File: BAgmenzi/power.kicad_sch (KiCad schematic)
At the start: 37 parts, among them J2 DF52-2S-0.8H(21), J3 USB3076-30-A, U10 PESD1USB30, U11 MAX77654BENV+T, U13 TPS7A2033DBVDQN, U14 TPS63900

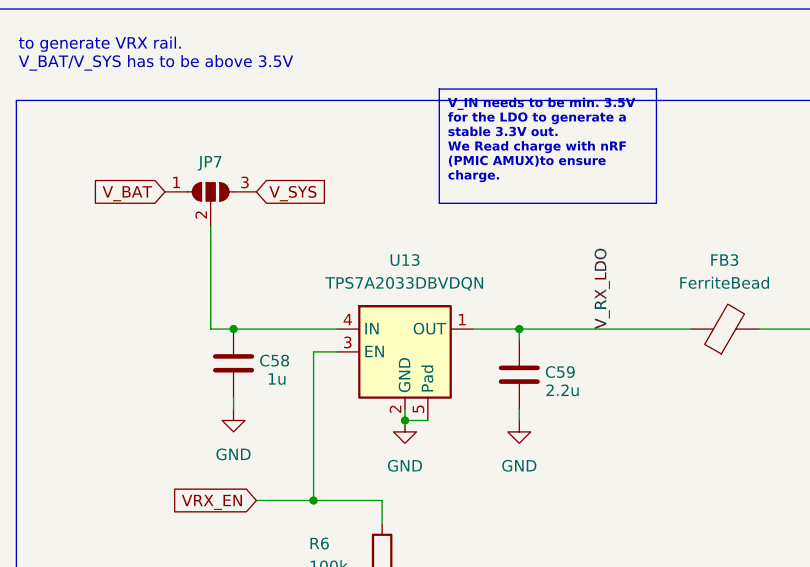
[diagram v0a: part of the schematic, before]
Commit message: LCSC parts complete, changed L5andL6 footprint
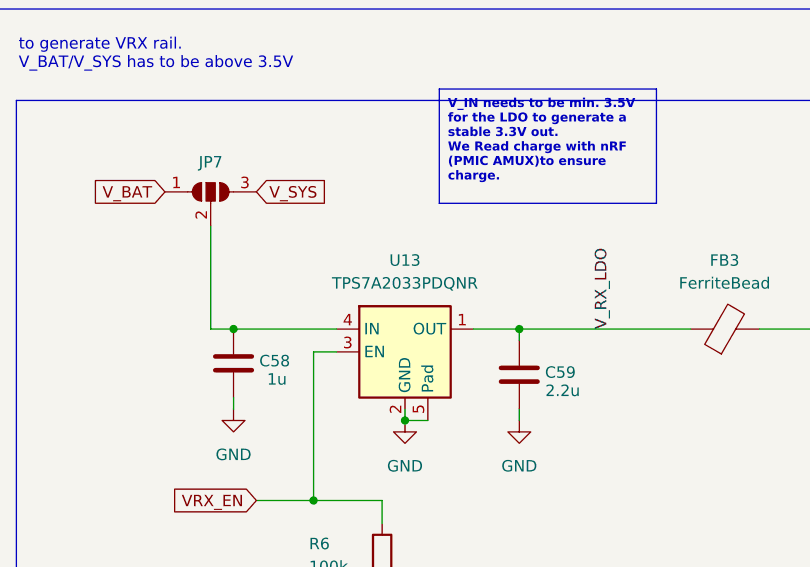
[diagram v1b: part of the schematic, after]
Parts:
- C32: LCSC Part # C161362 -> C169842
- C47, C52, C54: LCSC Part # (none) -> C105226
- C49, C51, C58: LCSC Part # C20441333 -> C14445
- C53: LCSC Part # C2190182 -> C26404
- C56: LCSC Part # C15525 -> (none)
- C59: LCSC Part # C12530 -> C77002
- C60: LCSC Part # C1713 -> C408132
- D4: LCSC Part # C145508 -> C145508
- FB3: footprint PCB1:FP-BLM18-0_15-t0_8-IPC_A -> Inductor_SMD:L_0603_1608Metric; LCSC Part # (none) -> C3717002
- J2: LCSC Part # C82431 -> C82431
- J3: LCSC Part # C6007475 -> C6007475
- L7: LCSC Part # (none) -> C2891571
- R32, R33: LCSC Part # C423829 -> C25900
- R34, R35, R6: LCSC Part # C723496 -> C192169
- R36: LCSC Part # C270305 -> C191984
- RT1: LCSC Part # (none) -> C77131
- S1: LCSC Part # C2760983 -> C2760983
- U13: value TPS7A2033DBVDQN -> TPS7A2033PDQNR; LCSC Part # (none) -> C2871641
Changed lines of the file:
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@@
 			)
 		)
-		(property "LCSC Part #" "C2190182"
+		(property "LCSC Part #" "C26404 "
 			(at 213.36 146.05 90)
 			(effects
@@
 			)
 		)
-		(property "LCSC Part #" "C723496"
+		(property "LCSC Part #" "C192169 "
 			(at 68.58 154.94 0)
 			(effects
@@
 			)
 		)
-		(property "Value" "TPS7A2033DBVDQN"
+		(property "Value" "TPS7A2033PDQNR"
 			(at 170.18 238.76 0)
 			(effects
@@
 			)
 		)
+		(property "LCSC Part #" "C2871641 "
+			(at 170.18 246.38 0)
+			(effects
+				(font
+					(size 1.27 1.27)
+				)
+				(hide yes)
+			)
+		)
 		(pin "4"
 		)
@@
 			)
 		)
-		(property "LCSC Part #" "C145508"
+		(property "LCSC Part #" "C145508 "
 			(at 105.41 43.18 0)
 			(effects
@@
 			)
 		)
-		(property "LCSC Part #" "C12530"
+		(property "LCSC Part #" "C77002 "
 			(at 182.88 248.92 0)
 			(effects
@@
 			)
 		)
-		(property "LCSC Part #" "C1713"
+		(property "LCSC Part #" "C408132 "
 			(at 219.71 252.73 0)
 			(effects
@@
 			)
 		)
+		(property "LCSC Part #" "C105226 "
+			(at 193.04 137.16 0)
+			(effects
+				(font
+					(size 1.27 1.27)
+				)
+				(hide yes)
+			)
+		)
 		(pin "2"
 		)
@@
 			)
 		)
-		(property "Footprint" "PCB1:FP-BLM18-0_15-t0_8-IPC_A"
+		(property "Footprint" "Inductor_SMD:L_0603_1608Metric"
 			(at 205.74 245.618 90)
 			(effects
@@
 			)
 		)
+		(property "LCSC Part #" "C3717002 "
+			(at 205.74 243.84 90)
+			(effects
+				(font
+					(size 1.27 1.27)
+				)
+				(hide yes)
+			)
+		)
 		(pin "1"
 		)
@@
 			)
 		)
+		(property "LCSC Part #" "C77131 "
+			(at 154.94 173.99 0)
+			(effects
+				(font
+					(size 1.27 1.27)
+				)
+				(hide yes)
+			)
+		)
 		(pin "1"
 		)
@@
 			)
 		)
+		(property "LCSC Part #" "C105226 "
+			(at 278.13 123.19 90)
+			(effects
+				(font
+					(size 1.27 1.27)
+				)
+				(hide yes)
+			)
+		)
 		(pin "2"
 		)
@@
 			)
 		)
-		(property "LCSC Part #" "C723496"
+		(property "LCSC Part #" "C192169 "
 			(at 167.64 269.24 0)
 			(effects
@@
 			)
 		)
-		(property "LCSC Part #" "C15525"
+		(property "LCSC Part #" ""
 			(at 54.61 323.85 0)
 			(effects
@@
 			)
 		)
-		(property "LCSC Part #" "C6007475"
+		(property "LCSC Part #" "C6007475 "
 			(at 142.24 52.07 0)
 			(effects
@@
 			)
 		)
-		(property "LCSC Part #" "C20441333"
+		(property "LCSC Part #" "C14445 "
 			(at 265.43 127 0)
 			(effects
@@
 			)
 		)
-		(property "LCSC Part #" "C423829"
+		(property "LCSC Part #" "C25900 "
 			(at 96.52 153.67 0)
 			(effects
@@
 			)
 		)
-		(property "LCSC Part #" "C2760983"
+		(property "LCSC Part #" "C2760983 "
 			(at 69.85 184.15 0)
 			(effects
@@
 			)
 		)
-		(property "LCSC Part #" "C82431"
+		(property "LCSC Part #" "C82431 "
 			(at 198.12 36.83 0)
 			(effects
@@
 			)
 		)
-		(property "LCSC Part #" "C20441333"
+		(property "LCSC Part #" "C14445 "
 			(at 151.13 247.65 0)
 			(effects
@@
 			)
 		)
-		(property "LCSC Part #" "C723496"
+		(property "LCSC Part #" "C192169 "
 			(at 58.42 154.94 0)
 			(effects
@@
 			)
 		)
-		(property "LCSC Part #" "C270305"
+		(property "LCSC Part #" "C191984 "
 			(at 156.21 166.37 90)
 			(effects
@@
 			)
 		)
+		(property "LCSC Part #" "C2891571 "
+			(at 213.36 138.43 0)
+			(effects
+				(font
+					(size 1.27 1.27)
+				)
+				(hide yes)
+			)
+		)
 		(pin "1"
 		)
@@
 			)
 		)
-		(property "LCSC Part #" "C20441333"
+		(property "LCSC Part #" "C14445 "
 			(at 158.75 129.54 0)
 			(effects
@@
 			)
 		)
-		(property "LCSC Part #" "C161362"
+		(property "LCSC Part #" "C169842 "
 			(at 279.4 152.4 0)
 			(effects
@@
 			)
 		)
-		(property "LCSC Part #" "C423829"
+		(property "LCSC Part #" "C25900 "
 			(at 101.6 153.67 0)
 			(effects
@@
 			(at 269.24 152.4 0)
 			(effects
+				(font
+					(size 1.27 1.27)
+				)
+				(hide yes)
+			)
+		)
+		(property "LCSC Part #" "C105226 "
+			(at 269.24 152.4 0)
+			(effects

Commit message: corrected LCSC numbers, other changes, Testpoints
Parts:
- added DVDD1, VRX1: TestPoint, TestPoint:TestPoint_Pad_D1.0mm, symbol Connector:TestPoint
- C32: LCSC Part # C169842 -> C1525
- C47, C52, C54: LCSC Part # C105226 -> C105226
- C49, C51, C58: LCSC Part # C14445 -> C14445
- C53: LCSC Part # C26404 -> C26404
- C59: LCSC Part # C77002 -> C77002
- C60: LCSC Part # C408132 -> C408132
- D4: LCSC Part # C145508 -> C145508
- FB3: LCSC Part # C3717002 -> C3717002
- J2: LCSC Part # C82431 -> C82431
- J3: LCSC Part # C6007475 -> C6007475
- L7: LCSC Part # C2891571 -> C2891571
- R32, R33: LCSC Part # C25900 -> C25900
- R34, R35, R6: LCSC Part # C192169 -> C192169
- R36: LCSC Part # C191984 -> C191984
- RT1: LCSC Part # C77131 -> C77131
- S1: LCSC Part # C2760983 -> C2760983
- U13: LCSC Part # C2871641 -> C2871641
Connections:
- net DVDD_3.3: now also DVDD1.1
- net V_RX: now also VRX1.1
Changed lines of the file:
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@@
 	)
 	(junction
+		(at 273.05 107.95)
+		(diameter 0)
+		(color 0 0 0 0)
+	)
+	(junction
 		(at 58.42 166.37)
 		(diameter 0)
@@
 	)
 	(junction
+		(at 236.22 243.84)
+		(diameter 0)
+		(color 0 0 0 0)
+	)
+	(junction
 		(at 160.02 262.89)
 		(diameter 0)
@@
 	)
 	(junction
+		(at 273.05 114.3)
+		(diameter 0)
+		(color 0 0 0 0)
+	)
+	(junction
 		(at 203.2 140.97)
 		(diameter 0)
@@
 	(wire
 		(pts
+			(xy 236.22 243.84) (xy 243.84 243.84)
+		)
+		(stroke
+			(width 0)
+			(type default)
+		)
+	)
+	(wire
+		(pts
 			(xy 58.42 166.37) (xy 107.95 166.37)
 		)
@@
 	(wire
 		(pts
-			(xy 162.56 118.11) (xy 148.59 118.11)
+			(xy 148.59 118.11) (xy 162.56 118.11)
 		)
 		(stroke
@@
 	(wire
 		(pts
+			(xy 273.05 107.95) (xy 273.05 105.41)
+		)
+		(stroke
+			(width 0)
+			(type default)
+		)
+	)
+	(wire
+		(pts
 			(xy 72.39 52.07) (xy 59.69 52.07)
 		)
@@
 	(wire
 		(pts
-			(xy 219.71 243.84) (xy 243.84 243.84)
+			(xy 219.71 243.84) (xy 236.22 243.84)
 		)
 		(stroke
@@
 	(wire
 		(pts
+			(xy 273.05 107.95) (xy 273.05 114.3)
+		)
+		(stroke
+			(width 0)
+			(type default)
+		)
+	)
+	(wire
+		(pts
 			(xy 142.24 58.42) (xy 142.24 57.15)
 		)
@@
 	(wire
 		(pts
+			(xy 271.78 114.3) (xy 273.05 114.3)
+		)
+		(stroke
+			(width 0)
+			(type default)
+		)
+	)
+	(wire
+		(pts
 			(xy 106.68 344.17) (xy 106.68 346.71)
 		)
@@
 	(wire
 		(pts
-			(xy 273.05 123.19) (xy 273.05 105.41)
+			(xy 273.05 123.19) (xy 273.05 114.3)
 		)
 		(stroke
@@
 	)
 	(label "DVDD_3.3"
-		(at 273.05 110.49 180)
+		(at 271.78 114.3 180)
 		(effects
 			(font
@@
 			)
 		)
-		(property "LCSC Part #" "C26404 "
+		(property "LCSC Part #" "C26404"
 			(at 213.36 146.05 90)
 			(effects
@@
 			)
 		)
-		(property "LCSC Part #" "C192169 "
+		(property "LCSC Part #" "C192169"
 			(at 68.58 154.94 0)
 			(effects
@@
 	)
 	(symbol
+		(lib_id "Connector:TestPoint")
+		(at 236.22 243.84 0)
+		(unit 1)
+		(exclude_from_sim no)
+		(in_bom yes)
+		(on_board yes)
+		(dnp no)
+		(fields_autoplaced yes)
+		(property "Reference" "VRX1"
+			(at 238.76 239.2679 0)
+			(effects
+				(font
+					(size 1.27 1.27)
+				)
+				(justify left)
+			)
+		)
+		(property "Value" "TestPoint"
+			(at 238.76 241.8079 0)
+			(effects
+				(font
+					(size 1.27 1.27)
+				)
+				(justify left)
+			)
+		)
+		(property "Footprint" "TestPoint:TestPoint_Pad_D1.0mm"
+			(at 241.3 243.84 0)
+			(effects
+				(font
+					(size 1.27 1.27)
+				)
+				(hide yes)
+			)
+		)
+		(property "Datasheet" "~"
+			(at 241.3 243.84 0)
+			(effects
+				(font
+					(size 1.27 1.27)
+				)
+				(hide yes)
+			)
+		)
+		(property "Description" "test point"
+			(at 236.22 243.84 0)
+			(effects
+				(font
+					(size 1.27 1.27)
+				)
+				(hide yes)
+			)
+		)
+		(pin "1"
+		)
+		(instances
+			(project ""
+				(path "/8cc4acae-3f14-463c-b0a0-3bc1c8d05954/d463870e-9fcf-4af5-ace7-dfb7bf5f63b9"
+					(reference "VRX1")
+					(unit 1)
+				)
+			)
+		)
+	)
+	(symbol
 		(lib_id "EEG_SchLib:MAX77654BENV+T")
 		(at 243.84 135.89 0)
@@
 			)
 		)
-		(property "LCSC Part #" "C2871641 "
+		(property "LCSC Part #" "C2871641"
 			(at 170.18 246.38 0)
 			(effects
@@
 			)
 		)
-		(property "LCSC Part #" "C145508 "
+		(property "LCSC Part #" "C145508"
 			(at 105.41 43.18 0)
 			(effects
@@
 			)
 		)
-		(property "LCSC Part #" "C77002 "
+		(property "LCSC Part #" "C77002"
 			(at 182.88 248.92 0)
 			(effects
@@
 			)
 		)
-		(property "LCSC Part #" "C408132 "
+		(property "LCSC Part #" "C408132"
 			(at 219.71 252.73 0)
 			(effects
@@
 			)
 		)
-		(property "LCSC Part #" "C105226 "
+		(property "LCSC Part #" "C105226"
 			(at 193.04 137.16 0)
 			(effects
@@
 			)
 		)
-		(property "LCSC Part #" "C3717002 "
+		(property "LCSC Part #" "C3717002"
 			(at 205.74 243.84 90)
 			(effects
@@
 	)
 	(symbol
+		(lib_id "Connector:TestPoint")
+		(at 273.05 107.95 90)
+		(unit 1)
+		(exclude_from_sim no)
+		(in_bom yes)
+		(on_board yes)
+		(dnp no)
+		(fields_autoplaced yes)
+		(property "Reference" "DVDD1"
+			(at 269.748 102.87 90)
+			(effects
+				(font
+					(size 1.27 1.27)
+				)
+			)
+		)
+		(property "Value" "TestPoint"
+			(at 269.748 105.41 90)
+			(effects
+				(font
+					(size 1.27 1.27)
+				)
+			)
+		)
+		(property "Footprint" "TestPoint:TestPoint_Pad_D1.0mm"
+			(at 273.05 102.87 0)
+			(effects
+				(font
+					(size 1.27 1.27)
+				)
+				(hide yes)
+			)
+		)
+		(property "Datasheet" "~"
+			(at 273.05 102.87 0)
+			(effects
+				(font
+					(size 1.27 1.27)
+				)
+				(hide yes)
+			)
+		)
+		(property "Description" "test point"
+			(at 273.05 107.95 0)
+			(effects
+				(font
+					(size 1.27 1.27)
+				)
+				(hide yes)
+			)
+		)
+		(pin "1"
+		)
+		(instances
+			(project "BAgmenzi"
+				(path "/8cc4acae-3f14-463c-b0a0-3bc1c8d05954/d463870e-9fcf-4af5-ace7-dfb7bf5f63b9"
+					(reference "DVDD1")
+					(unit 1)
+				)
+			)
+		)
+	)
+	(symbol
 		(lib_id "Device:R")
 		(at 95.25 350.52 180)
@@
 			)
 		)
-		(property "LCSC Part #" "C77131 "
+		(property "LCSC Part #" "C77131"
 			(at 154.94 173.99 0)
 			(effects
@@
 			)
 		)
-		(property "LCSC Part #" "C105226 "
+		(property "LCSC Part #" "C105226"
 			(at 278.13 123.19 90)
 			(effects
@@
 			)
 		)
-		(property "LCSC Part #" "C192169 "
+		(property "LCSC Part #" "C192169"
 			(at 167.64 269.24 0)
 			(effects
@@
 			)
 		)
-		(property "LCSC Part #" "C6007475 "
+		(property "LCSC Part #" "C6007475"
 			(at 142.24 52.07 0)
 			(effects
@@
 			)
 		)
-		(property "LCSC Part #" "C14445 "
+		(property "LCSC Part #" "C14445"
 			(at 265.43 127 0)
 			(effects
@@
 			)
 		)
-		(property "LCSC Part #" "C25900 "
+		(property "LCSC Part #" "C25900"
 			(at 96.52 153.67 0)
 			(effects
@@
 			)
 		)
-		(property "LCSC Part #" "C2760983 "
+		(property "LCSC Part #" "C2760983"
 			(at 69.85 184.15 0)
 			(effects
@@
 			)
 		)
-		(property "LCSC Part #" "C82431 "
+		(property "LCSC Part #" "C82431"
 			(at 198.12 36.83 0)
 			(effects
@@
 			)
 		)
-		(property "LCSC Part #" "C14445 "
+		(property "LCSC Part #" "C14445"
 			(at 151.13 247.65 0)
 			(effects
@@
 			)
 		)
-		(property "LCSC Part #" "C192169 "
+		(property "LCSC Part #" "C192169"
 			(at 58.42 154.94 0)
 			(effects
@@
 			)
 		)
-		(property "LCSC Part #" "C191984 "
+		(property "LCSC Part #" "C191984"
 			(at 156.21 166.37 90)
 			(effects
@@
 			)
 		)
-		(property "LCSC Part #" "C2891571 "
+		(property "LCSC Part #" "C2891571"
 			(at 213.36 138.43 0)
 			(effects
@@
 			)
 		)
-		(property "LCSC Part #" "C14445 "
+		(property "LCSC Part #" "C14445"
 			(at 158.75 129.54 0)
 			(effects
@@
 			)
 		)
-		(property "LCSC Part #" "C169842 "
+		(property "LCSC Part #" "C1525"
 			(at 279.4 152.4 0)
 			(effects
@@
 			)
 		)
-		(property "LCSC Part #" "C25900 "
+		(property "LCSC Part #" "C25900"
 			(at 101.6 153.67 0)
 			(effects
@@
 			)
 		)
-		(property "LCSC Part #" "C105226 "
+		(property "LCSC Part #" "C105226"
 			(at 269.24 152.4 0)
 			(effects

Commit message: small changes
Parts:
- added VLED1: TestPoint, TestPoint:TestPoint_Pad_D1.0mm, symbol Connector:TestPoint
- DVDD1, VRX1: now left out of the parts list
- U10: now not fitted
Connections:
- net V_LED: now also VLED1.1
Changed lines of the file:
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@@
 	)
 	(junction
+		(at 280.67 140.97)
+		(diameter 0)
+		(color 0 0 0 0)
+	)
+	(junction
 		(at 97.79 123.19)
 		(diameter 0)
@@
 	(wire
 		(pts
+			(xy 280.67 140.97) (xy 283.21 140.97)
+		)
+		(stroke
+			(width 0)
+			(type default)
+		)
+	)
+	(wire
+		(pts
 			(xy 78.74 143.51) (xy 78.74 163.83)
 		)
@@
 	(wire
 		(pts
-			(xy 279.4 140.97) (xy 283.21 140.97)
+			(xy 279.4 140.97) (xy 280.67 140.97)
 		)
 		(stroke
@@
 		(in_bom yes)
 		(on_board yes)
-		(dnp no)
+		(dnp yes)
 		(property "Reference" "U10"
 			(at 103.886 68.072 0)
@@
 		(unit 1)
 		(exclude_from_sim no)
-		(in_bom yes)
+		(in_bom no)
 		(on_board yes)
 		(dnp no)
@@
 		(unit 1)
 		(exclude_from_sim no)
-		(in_bom yes)
+		(in_bom no)
 		(on_board yes)
 		(dnp no)
@@
 					(unit 1)
 				)
+			)
+		)
+	)
+	(symbol
+		(lib_id "Connector:TestPoint")
+		(at 280.67 140.97 0)
+		(unit 1)
+		(exclude_from_sim no)
+		(in_bom no)
+		(on_board yes)
+		(dnp no)
+		(fields_autoplaced yes)
+		(property "Reference" "VLED1"
+			(at 283.21 136.3979 0)
+			(effects
+				(font
+					(size 1.27 1.27)
+				)
+				(justify left)
+			)
+		)
+		(property "Value" "TestPoint"
+			(at 283.21 138.9379 0)
+			(effects
+				(font
+					(size 1.27 1.27)
+				)
+				(justify left)
+			)
+		)
+		(property "Footprint" "TestPoint:TestPoint_Pad_D1.0mm"
+			(at 285.75 140.97 0)
+			(effects
+				(font
+					(size 1.27 1.27)
+				)
+				(hide yes)
+			)
+		)
+		(property "Datasheet" "~"
+			(at 285.75 140.97 0)
+			(effects
+				(font
+					(size 1.27 1.27)
+				)
+				(hide yes)
+			)
+		)
+		(property "Description" "test point"
+			(at 280.67 140.97 0)
+			(effects
+				(font
+					(size 1.27 1.27)
+				)
+				(hide yes)
+			)
+		)
+		(pin "1"
+		)
+		(instances
+			(project "BAgmenzi"
+				(path "/8cc4acae-3f14-463c-b0a0-3bc1c8d05954/d463870e-9fcf-4af5-ace7-dfb7bf5f63b9"
+					(reference "VLED1")
+					(unit 1)
+				)
